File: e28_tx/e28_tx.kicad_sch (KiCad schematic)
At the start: 4 parts

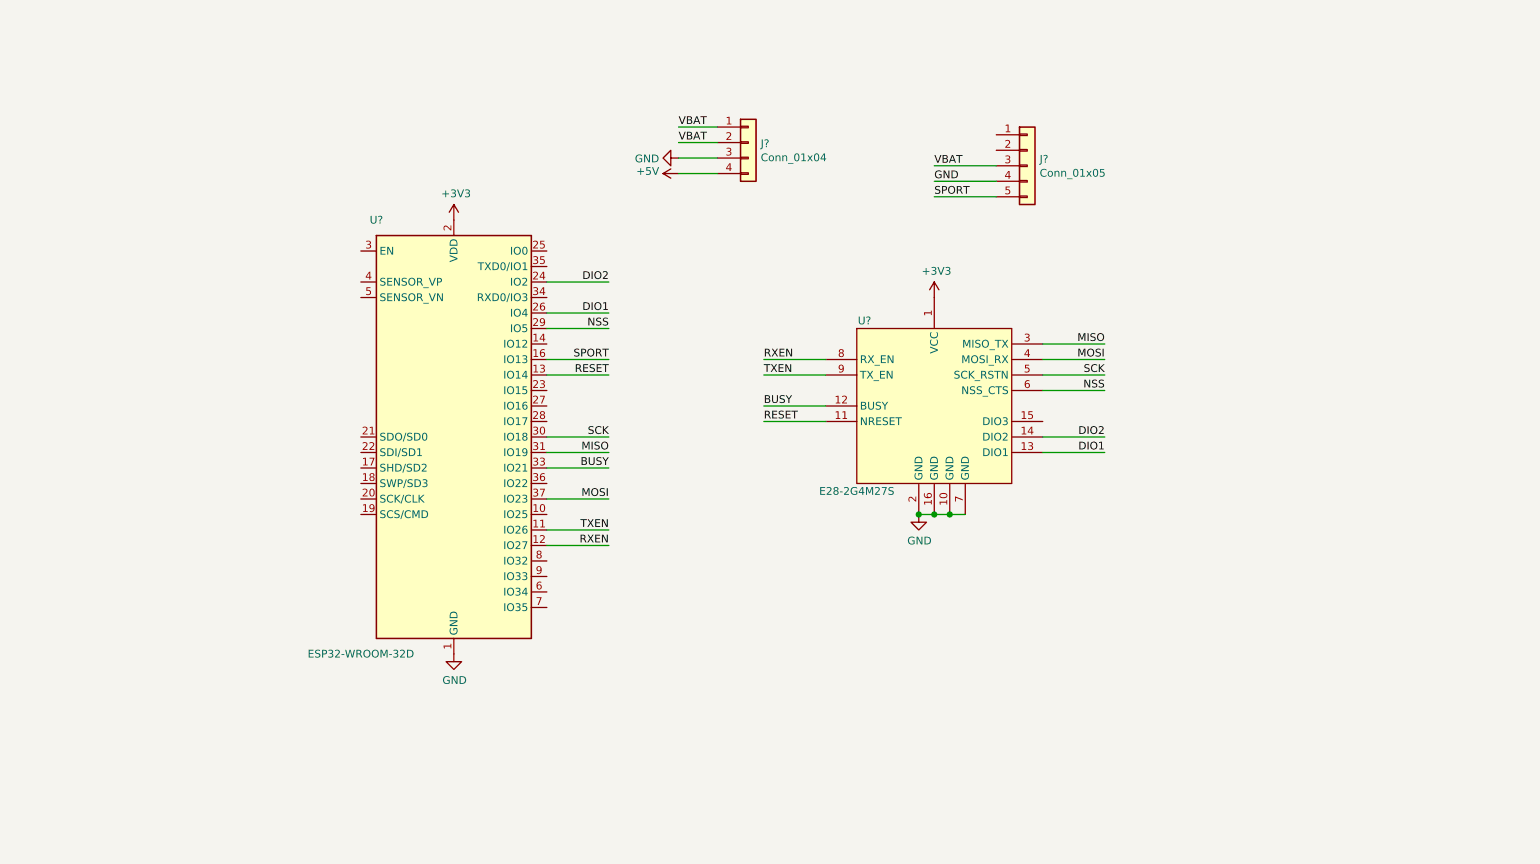
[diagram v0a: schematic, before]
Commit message: Finished TX and RX, added 3d models
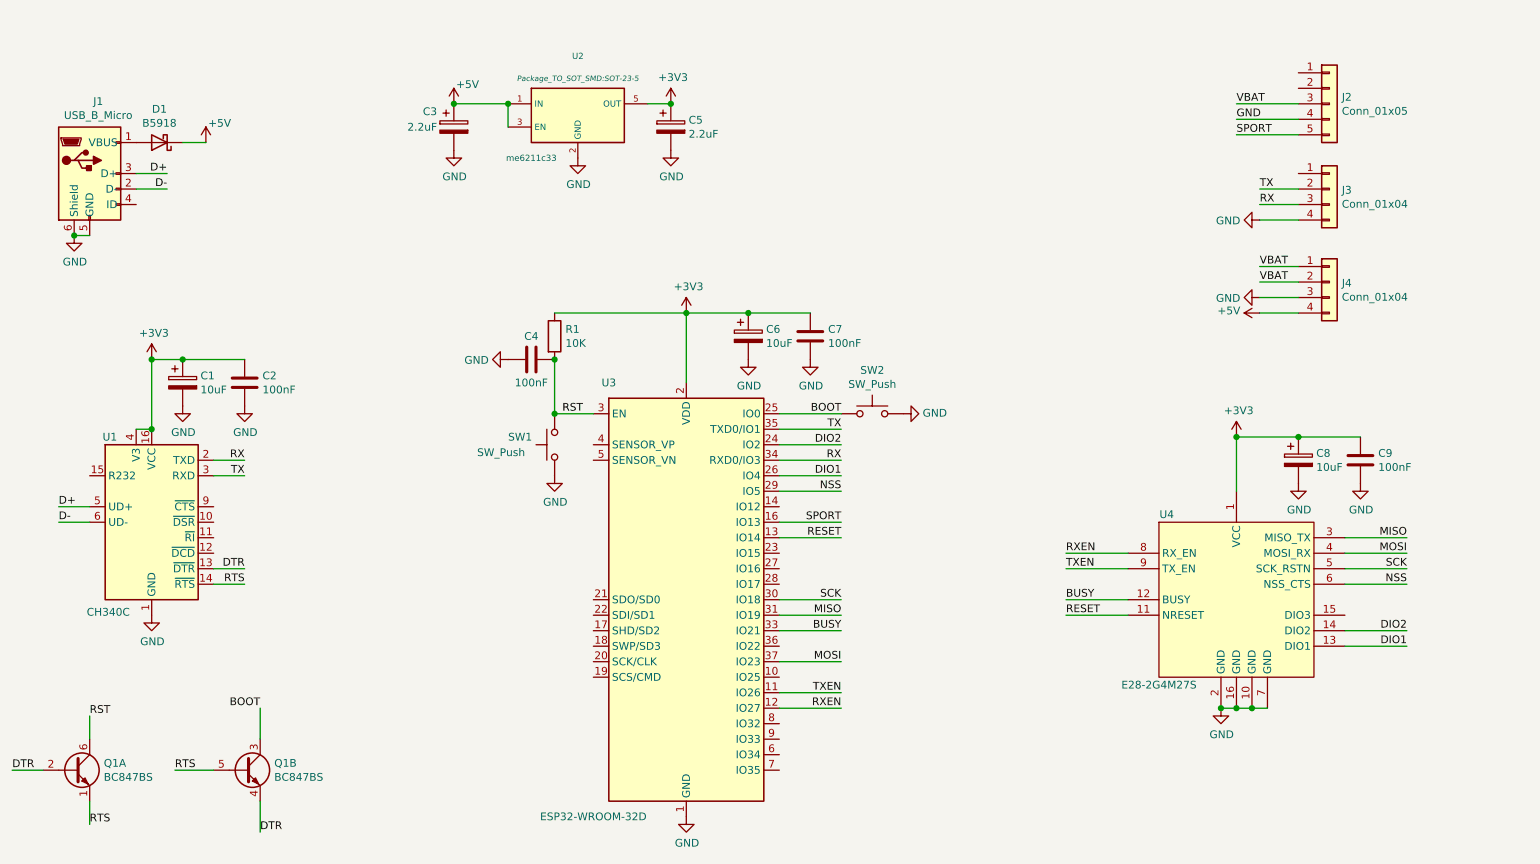
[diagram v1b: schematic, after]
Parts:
- added C1, C6, C8: 10uF, Capacitor_Tantalum_SMD:CP_EIA-1608-08_AVX-J_Pad1.25x1.05mm_HandSolder, symbol device:CP
- added C2, C4, C7, C9: 100nF, Capacitor_SMD:C_0603_1608Metric_Pad1.05x0.95mm_HandSolder, symbol device:C
- added C3, C5: 2.2uF, Capacitor_Tantalum_SMD:CP_EIA-1608-08_AVX-J_Pad1.25x1.05mm_HandSolder, symbol device:CP
- added D1: B5918, Diode_SMD:D_SOD-323_HandSoldering, symbol device:D_Schottky
- added J1: USB_B_Micro, Connector_USB:USB_Micro-B_Wuerth_614105150721_Vertical, symbol Connector:USB_B_Micro
- added J3: Conn_01x04, Connector_PinHeader_2.54mm:PinHeader_1x04_P2.54mm_Vertical, symbol Connector_Generic:Conn_01x04
- added Q1: BC847BS, Package_TO_SOT_SMD:SOT-363_SC-70-6, symbol Transistor_BJT:BC847BS
- added R1: 10K, Resistor_SMD:R_0603_1608Metric_Pad1.05x0.95mm_HandSolder, symbol device:R
- added SW1, SW2: SW_Push, Button_Switch_SMD:SW_SPST_TL3342, symbol Switch:SW_Push
- added U1: CH340C, Package_SO:SOIC-16_3.9x9.9mm_P1.27mm, symbol Interface_USB:CH340C
- added U2: me6211c33, Package_TO_SOT_SMD:SOT-23-5, symbol regul:TLV70012DDC
- J2: renamed from J?; footprint (none) -> ELRS_lib:MOLEX_0022142054
- J4: renamed from J?; footprint (none) -> Connector_PinHeader_2.54mm:PinHeader_1x04_P2.54mm_Vertical
- U4: renamed from U?; footprint (none) -> ELRS_lib:E28-2G4M27S
- gave numbers to parts that had none: 1
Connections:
- net +3V3: now also C1.1, C2.1, C5.1, C6.1, C7.1, C8.1, C9.1, R1.1, U1.16 (VCC), U1.4 (V3), U2.5 (OUT)
- net +5V: now also C3.1, D1.1 (K), U2.1 (IN), U2.3 (EN)
- net GND: now also C1.2, C2.2, C3.2, C4.1, C5.2, C6.2, C7.2, C8.2, C9.2, J1.5 (GND), J1.6 (Shield), J3.4 (Pin_4), SW1.1, SW2.2, U1.1 (GND), U2.2 (GND)
- net BOOT: now reaches U3.25 (IO0)
- net BOOT: now also Q1.3 (C2), SW2.1
- net RST: now reaches U3.3 (EN)
- net RST: now also C4.2, Q1.6 (C1), R1.2, SW1.2
- net RX: now reaches U3.34 (RXD0/IO3)
- net RX: now also J3.3 (Pin_3), U1.2 (TXD)
- net TX: now reaches U3.35 (TXD0/IO1)
- net TX: now also J3.2 (Pin_2), U1.3 (RXD)
- new net: D1.2 (A), J1.1 (VBUS)
- new net D+: J1.3 (D+), U1.5 (UD+)
- new net D-: J1.2 (D-), U1.6 (UD-)
- new net DTR: Q1.2 (B1), Q1.4 (E2), U1.13 (~DTR)
- new net RTS: Q1.1 (E1), Q1.5 (B2), U1.14 (~RTS)
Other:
- moved on the sheet: J2, J4, U3, U4

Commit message: Added minimal RX
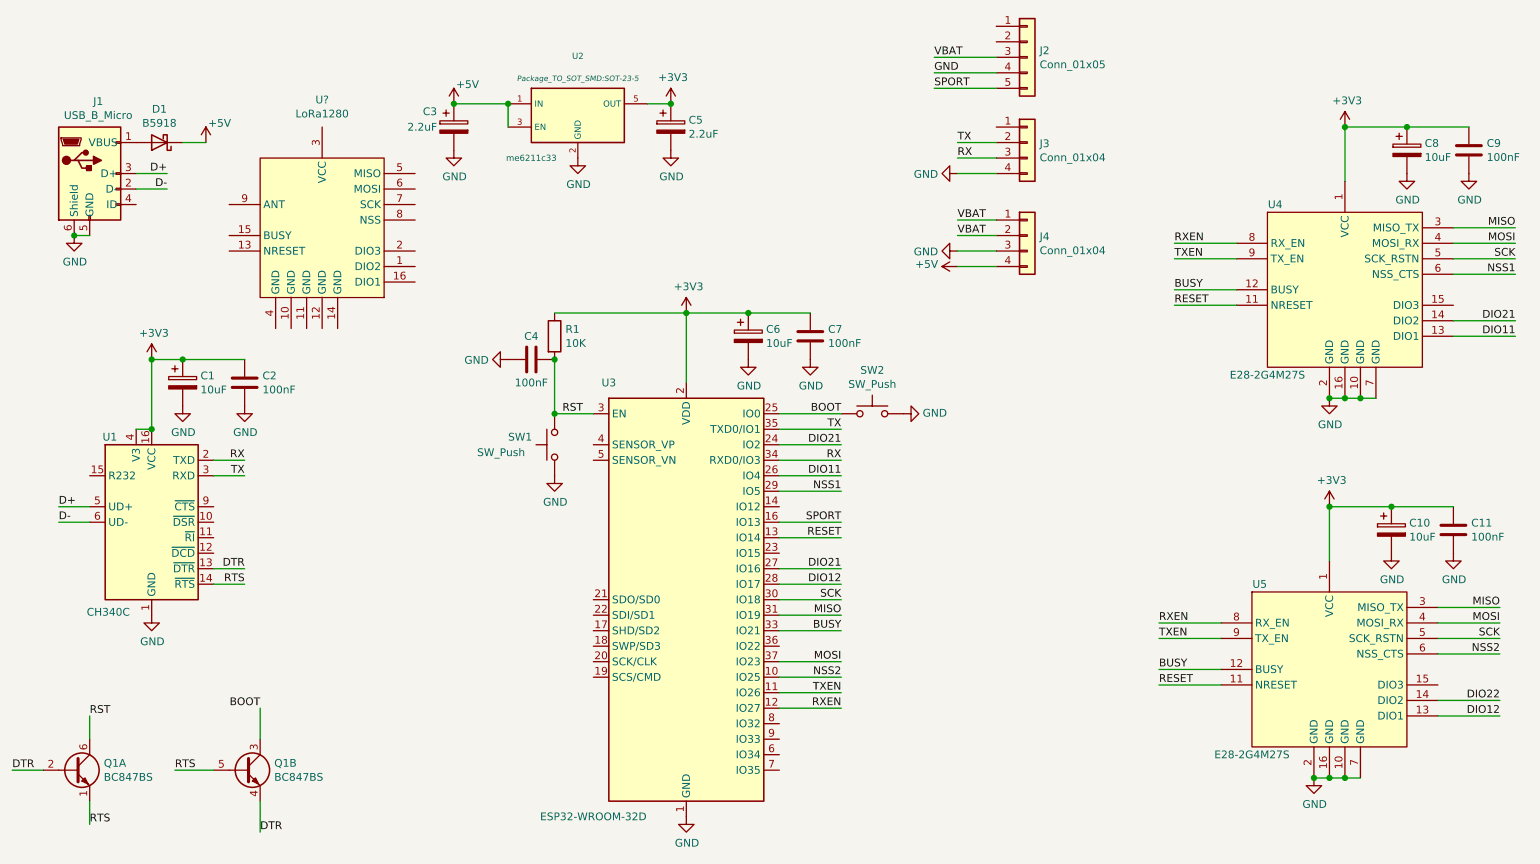
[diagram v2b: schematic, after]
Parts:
- added C10: 10uF, Capacitor_Tantalum_SMD:CP_EIA-1608-08_AVX-J_Pad1.25x1.05mm_HandSolder, symbol device:CP
- added C11: 100nF, Capacitor_SMD:C_0603_1608Metric_Pad1.05x0.95mm_HandSolder, symbol device:C
- added U5: E28-2G4M27S, ELRS_lib:E28-2G4M27S, symbol ELRS_lib:E28-2G4M27S
- added U?: LoRa1280, symbol ELRS_lib:LoRa1280
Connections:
- net DIO2 is gone; now on net DIO21: U3.24 (IO2), U4.14 (DIO2)
- net +3V3: now also C10.1, C11.1, U5.1 (VCC)
- net BUSY: now also U5.12 (BUSY)
- net GND: now also C10.2, C11.2, U5.10 (GND), U5.16 (GND), U5.2 (GND), U5.7 (GND)
- net MISO: now also U5.3 (MISO_TX)
- net MOSI: now also U5.4 (MOSI_RX)
- net RESET: now also U5.11 (NRESET)
- net RXEN: now also U5.8 (RX_EN)
- net SCK: now also U5.5 (SCK_RSTN)
- net TXEN: now also U5.9 (TX_EN)
- net NSS2: now reaches U3.10 (IO25)
- net NSS2: now also U5.6 (NSS_CTS)
- net DIO21: now reaches U3.27 (IO16)
- net DIO12: now reaches U3.28 (IO17)
- net DIO12: now also U5.13 (DIO1)
- net DIO1 renamed DIO11
- net NSS renamed NSS1
- new net DIO22: U5.14 (DIO2)
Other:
- moved on the sheet: C8, C9, J2, J3, J4, U4
